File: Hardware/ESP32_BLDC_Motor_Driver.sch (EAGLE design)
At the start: 125 parts, among them J1 USB-C Connector, J4 Breadboard Connector, J5 Breadboard Headers, J7 QWIIC_RIGHT_ANGLE, P1 0532610371, Q2 NPN Transistors, Q3 20V/4.2A/52mΩ/1.4W, U1 TMC6300, U2 3.3V, U3 ESP-WROOM-3232D, U4 CH340C, U5 ESD Diode, U6 AP63357, U8 TMAG5273, U9 LMV324

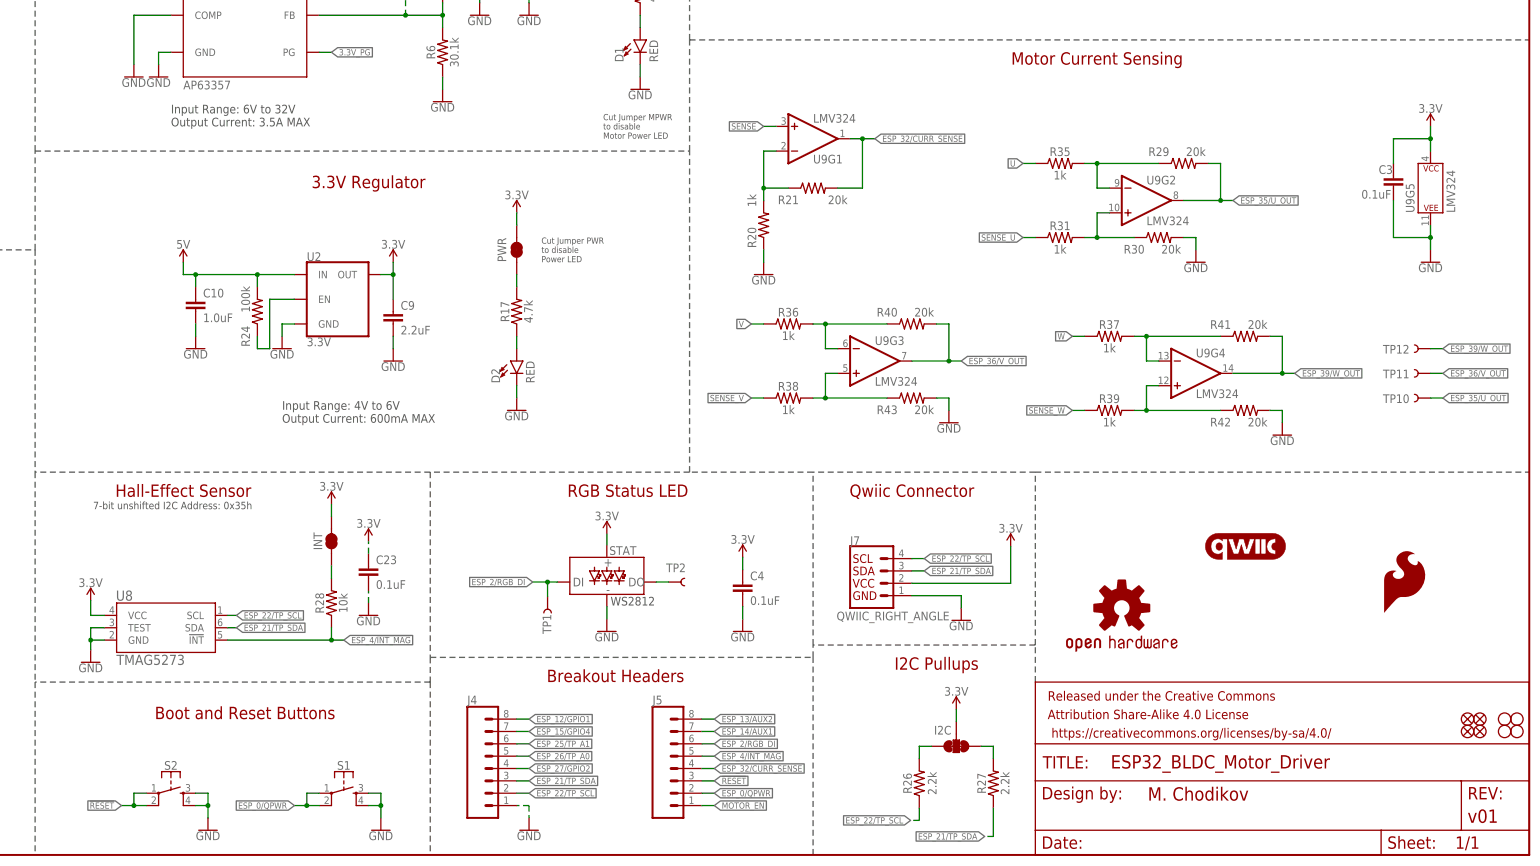
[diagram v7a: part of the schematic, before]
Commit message: V10 INITIAL COMMIT
Added datasheets for new parts; created new library component for the INA240 inline current sensing; lined up other parts for symmetry; redid the OPA344 current sensing section
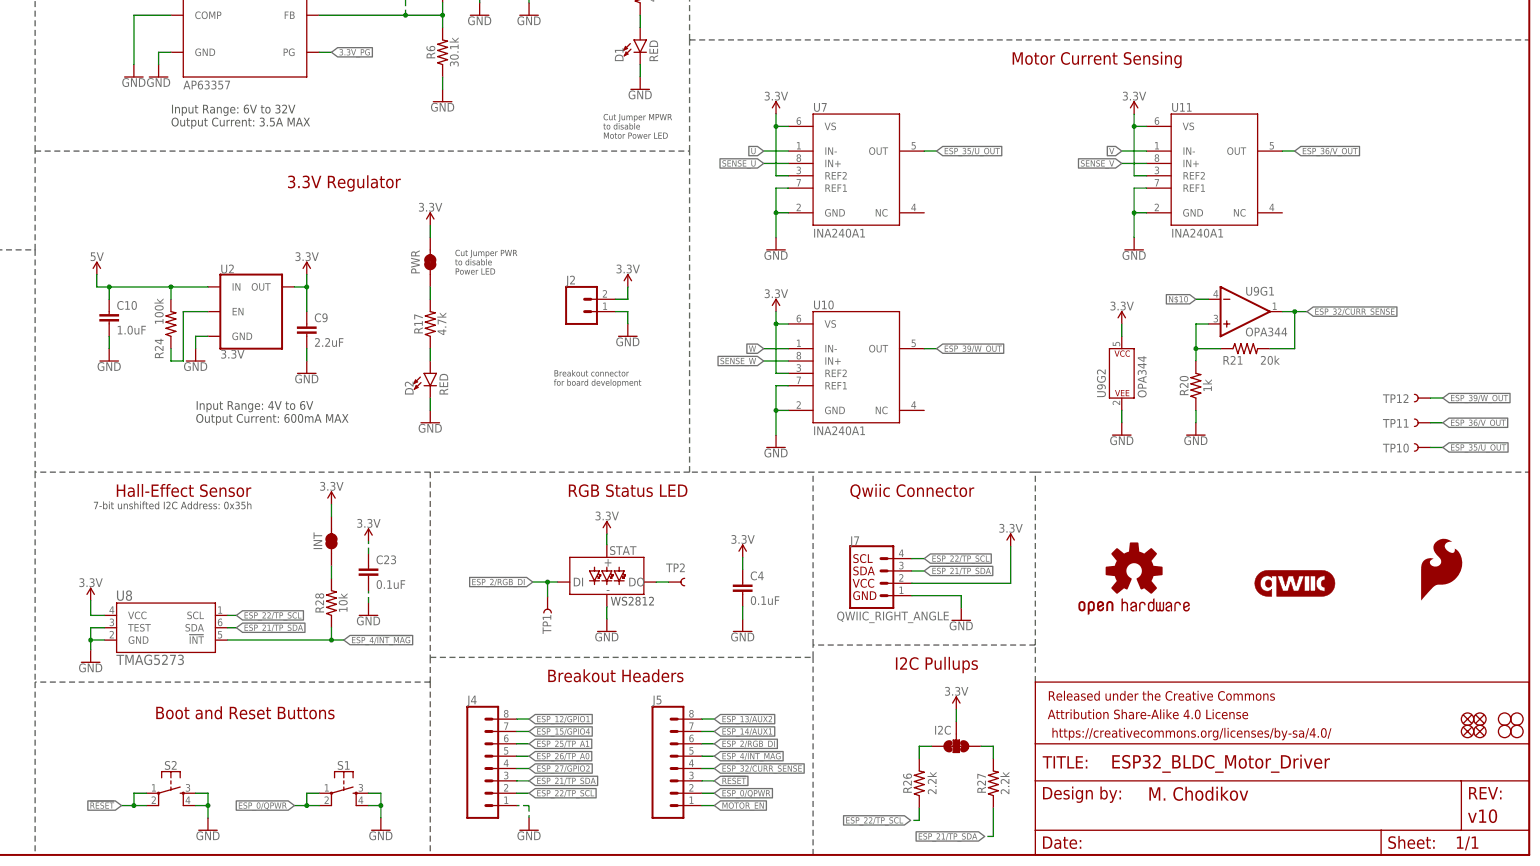
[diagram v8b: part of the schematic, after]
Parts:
- removed C3: 0.1uF, SparkFun-Capacitors:0.1UF-0603-25V-10%-X7R-WE
- removed R29, R30, R40, R41, R42, R43: 20k, SparkFun-Resistors:20KOHM-0603-1/10W-1%
- removed R31, R35, R36, R37, R38, R39: 1k, SparkFun-Resistors:1KOHM-0603-1/10W-1%
- added J2: (no value), SparkFun-Connectors:CONN_021X02_NO_SILK
- added U10, U11, U7: INA240A1, INA240A1:INA240A1D
- FRAME1: REV v01 -> v10
- U9: value LMV324 -> OPA344; device SparkFun-IC-Amplifiers:LMV324 -> SparkFun-IC-Amplifiers:OPA344
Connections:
- removed net N$16: R29.1, R35.2, U9G2.-IN
- removed net N$18: R30.1, R31.2, U9G2.+IN
- removed net N$19: R36.2, R40.1, U9G3.-IN
- removed net N$20: R38.2, R43.1, U9G3.+IN
- removed net N$24: R37.2, R41.1, U9G4.-IN
- removed net N$25: R39.2, R42.1, U9G4.+IN
- new net N$10: U9G1.-IN
- net 3.3V: now also J2.2, U10.REF2, U10.VS, U11.REF2, U11.VS, U7.REF2, U7.VS, U9G2.P$V+; no longer C3.1, U9G5.P$V+
- net ESP_35/U_OUT: now also U7.OUT; no longer R29.2, U9G2.OUT
- net ESP_36/V_OUT: now also U11.OUT; no longer R40.2, U9G3.OUT
- net ESP_39/W_OUT: now also U10.OUT; no longer R41.2, U9G4.OUT
- net GND: now also J2.1, U10.GND, U10.REF1, U11.GND, U11.REF1, U7.GND, U7.REF1, U9G2.P$V-; no longer C3.2, R30.2, R42.2, R43.2, U9G5.P$V-
- net N$14: now also U9G1.+IN; no longer U9G1.-IN
- net SENSE: no longer U9G1.+IN
- net SENSE_U: now also U7.IN+; no longer R31.1
- net SENSE_V: now also U11.IN+; no longer R38.1
- net SENSE_W: now also U10.IN+; no longer R39.1
- net U: now also U7.IN-; no longer R35.1
- net V: now also U11.IN-; no longer R36.1
- net W: now also U10.IN-; no longer R37.1
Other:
- note added: "Breakout connector for board development"
- moved on the sheet: C10, C9, D2, PWR, R17, R20, R21, R24, TP10, TP11, TP12, U2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
